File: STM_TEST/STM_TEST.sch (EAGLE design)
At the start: 49 parts, among them U1 TPS2115APWR, U2 AZ1117EH-3.3TRG1, Y1 ECS-80-S-4X, Y2 ECS-80-S-4X

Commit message: routing
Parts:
- removed C3, C4: 1.0uF, SparkFun-Capacitors:1.0UF-0603-16V-10%
- removed SW1: (no value), special:SW_DIP-2
- removed U2: AZ1117EH-3.3TRG1, AZ1117EH-3.3TRG1:AZ1117EH-3.3TRG1
- added R12: 10k, SparkFun-Resistors:100KOHM-0603-1/10W-1%
- added R13, R14: 10k, SparkFun-Resistors:1KOHM-0603-1/10W-1%
- R3, R4: device SparkFun-Resistors:100KOHM-0603-1/10W-1% -> SparkFun-Resistors:1KOHM-0603-1/10W-1%
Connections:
- removed net D1: R3.2, SW1.1, U1.D1
- removed net SCL: PCB1.GPIO3
- removed net SDA: PCB1.GPIO2
- removed net VCC: C3.1, J1.2, U2.IN
- new net +3V3ROV_ADC2: R3.1, R4.2, U$2.PA2
- new net +5V_ADC1: R13.1, R14.2, U$2.PA1
- net +3V3ROV: now also J1.2, R12.2, R3.2; no longer C4.1, R3.1, R4.1, U2.OUT
- net +5V: now also R13.2
- net D0: now also R12.1; no longer R4.2, SW1.2
- net GND: now also R14.1, R4.1, U1.D1; no longer C3.2, C4.2, SW1.3, SW1.4, U2.ADJ/GND
- net I2C1_SCL: now also PCB1.GPIO3
- net I2C1_SDA: now also PCB1.GPIO2

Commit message: uhhh, yeah boards looking good
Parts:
- added C3: 0.1uF, SparkFun-Capacitors:4.7UF0603
- added U$4: ACS711, ACS711_ameter:ACS711
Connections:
- new net +5V_TO_PI: U$4.IP1-, U$4.IP2-
- new net PI_CURRENT: U$2.PA0, U$4.VIOUT
- net +3V3: now also C3.1, U$4.VCC
- net +5V: now also U$4.IP1+, U$4.IP2+
- net GND: now also C3.2, U$4.GND
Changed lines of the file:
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@@
 <part name="R14" library="SparkFun-Resistors" library_urn="urn:adsk.eagle:library:532" deviceset="1KOHM" device="-0603-1/10W-1%" package3d_urn="urn:adsk.eagle:package:39650/1" value="10k"/>
 <part name="GND10" library="supply1" library_urn="urn:adsk.eagle:library:371" deviceset="GND" device=""/>
+<part name="U$4" library="ACS711_ameter" deviceset="ACS711" device=""/>
+<part name="C3" library="SparkFun-Capacitors" library_urn="urn:adsk.eagle:library:510" deviceset="4.7UF" device="0603" package3d_urn="urn:adsk.eagle:package:37414/1" value="0.1uF"/>
+<part name="GND17" library="supply1" library_urn="urn:adsk.eagle:library:371" deviceset="GND" device=""/>
+<part name="+3V7" library="supply1" library_urn="urn:adsk.eagle:library:371" deviceset="+3V3" device=""/>
 </parts>
 <sheets>
@@
 <instance part="GND10" gate="1" x="314.96" y="50.8">
 <attribute name="VALUE" x="312.42" y="48.26" size="1.778" layer="96"/>
+</instance>
+<instance part="U$4" gate="G$1" x="210.82" y="53.34"/>
+<instance part="C3" gate="G$1" x="251.46" y="53.34">
+<attribute name="NAME" x="252.984" y="56.261" size="1.778" layer="95" font="vector"/>
+<attribute name="VALUE" x="252.984" y="51.181" size="1.778" layer="96" font="vector"/>
+</instance>
+<instance part="GND17" gate="1" x="251.46" y="40.64">
+<attribute name="VALUE" x="248.92" y="38.1" size="1.778" layer="96"/>
+</instance>
+<instance part="+3V7" gate="G$1" x="251.46" y="78.74">
+<attribute name="VALUE" x="248.92" y="73.66" size="1.778" layer="96" rot="R90"/>
 </instance>
 </instances>
@@
 <wire x1="314.96" y1="60.96" x2="314.96" y2="53.34" width="0.1524" layer="91"/>
 </segment>
+<segment>
+<pinref part="C3" gate="G$1" pin="2"/>
+<pinref part="GND17" gate="1" pin="GND"/>
+<wire x1="251.46" y1="50.8" x2="251.46" y2="45.72" width="0.1524" layer="91"/>
+<pinref part="U$4" gate="G$1" pin="GND"/>
+<wire x1="251.46" y1="45.72" x2="251.46" y2="43.18" width="0.1524" layer="91"/>
+<wire x1="223.52" y1="45.72" x2="251.46" y2="45.72" width="0.1524" layer="91"/>
+<junction x="251.46" y="45.72"/>
+</segment>
 </net>
 <net name="+3V3" class="0">
@@
 <junction x="45.72" y="58.42"/>
 </segment>
+<segment>
+<pinref part="U$4" gate="G$1" pin="VCC"/>
+<pinref part="C3" gate="G$1" pin="1"/>
+<wire x1="223.52" y1="60.96" x2="251.46" y2="60.96" width="0.1524" layer="91"/>
+<wire x1="251.46" y1="60.96" x2="251.46" y2="58.42" width="0.1524" layer="91"/>
+<pinref part="+3V7" gate="G$1" pin="+3V3"/>
+<wire x1="251.46" y1="60.96" x2="251.46" y2="76.2" width="0.1524" layer="91"/>
+<junction x="251.46" y="60.96"/>
+</segment>
 </net>
 <net name="NRST" class="0">
@@
 <label x="314.96" y="96.52" size="1.778" layer="95"/>
 </segment>
+<segment>
+<pinref part="U$4" gate="G$1" pin="IP1+"/>
+<pinref part="U$4" gate="G$1" pin="IP2+"/>
+<wire x1="198.12" y1="60.96" x2="198.12" y2="55.88" width="0.1524" layer="91"/>
+<wire x1="198.12" y1="60.96" x2="177.8" y2="60.96" width="0.1524" layer="91"/>
+<junction x="198.12" y="60.96"/>
+<label x="177.8" y="60.96" size="1.778" layer="95"/>
+</segment>
 </net>
 <net name="+3V3ROV" class="0">
@@
 <wire x1="347.98" y1="96.52" x2="347.98" y2="86.36" width="0.1524" layer="91"/>
 <label x="347.98" y="96.52" size="1.778" layer="95"/>
+</segment>
+</net>
+<net name="PI_CURRENT" class="0">
+<segment>
+<pinref part="U$2" gate="G$1" pin="PA0"/>
+<wire x1="264.16" y1="203.2" x2="248.92" y2="203.2" width="0.1524" layer="91"/>
+<label x="243.84" y="203.2" size="1.778" layer="95"/>
+</segment>
+<segment>
+<pinref part="U$4" gate="G$1" pin="VIOUT"/>
+<wire x1="223.52" y1="55.88" x2="243.84" y2="55.88" width="0.1524" layer="91"/>
+<label x="231.14" y="55.88" size="1.778" layer="95"/>
+</segment>
+</net>
+<net name="+5V_TO_PI" class="0">
+<segment>
+<pinref part="U$4" gate="G$1" pin="IP1-"/>
+<pinref part="U$4" gate="G$1" pin="IP2-"/>
+<wire x1="198.12" y1="50.8" x2="198.12" y2="45.72" width="0.1524" layer="91"/>
+<wire x1="198.12" y1="45.72" x2="177.8" y2="45.72" width="0.1524" layer="91"/>
+<junction x="198.12" y="45.72"/>
+<label x="177.8" y="45.72" size="1.778" layer="95"/>
 </segment>
 </net>
@@
 <net name="+5V" class="0">
 <segment>
+<wire x1="40.64" y1="91.44" x2="40.64" y2="104.14" width="0.1524" layer="91"/>
+<pinref part="P+1" gate="1" pin="+5V"/>
+<pinref part="PCB1" gate="G$1" pin="5V@2"/>
+<wire x1="40.64" y1="91.44" x2="63.5" y2="91.44" width="0.1524" layer="91"/>
+</segment>
+<segment>
 <pinref part="PCB1" gate="G$1" pin="5V@4"/>
 <wire x1="63.5" y1="96.52" x2="58.42" y2="96.52" width="0.1524" layer="91"/>
-<wire x1="58.42" y1="96.52" x2="58.42" y2="93.98" width="0.1524" layer="91"/>
-<pinref part="PCB1" gate="G$1" pin="5V@2"/>
-<wire x1="58.42" y1="93.98" x2="58.42" y2="91.44" width="0.1524" layer="91"/>
-<wire x1="58.42" y1="91.44" x2="63.5" y2="91.44" width="0.1524" layer="91"/>
-<wire x1="58.42" y1="93.98" x2="40.64" y2="93.98" width="0.1524" layer="91"/>
-<wire x1="40.64" y1="93.98" x2="40.64" y2="104.14" width="0.1524" layer="91"/>
-<junction x="58.42" y="93.98"/>
-<pinref part="P+1" gate="1" pin="+5V"/>
-</segment>
-</net>
+<label x="55.88" y="96.52" size="1.778" layer="95"/>
+</segment>
+</net>

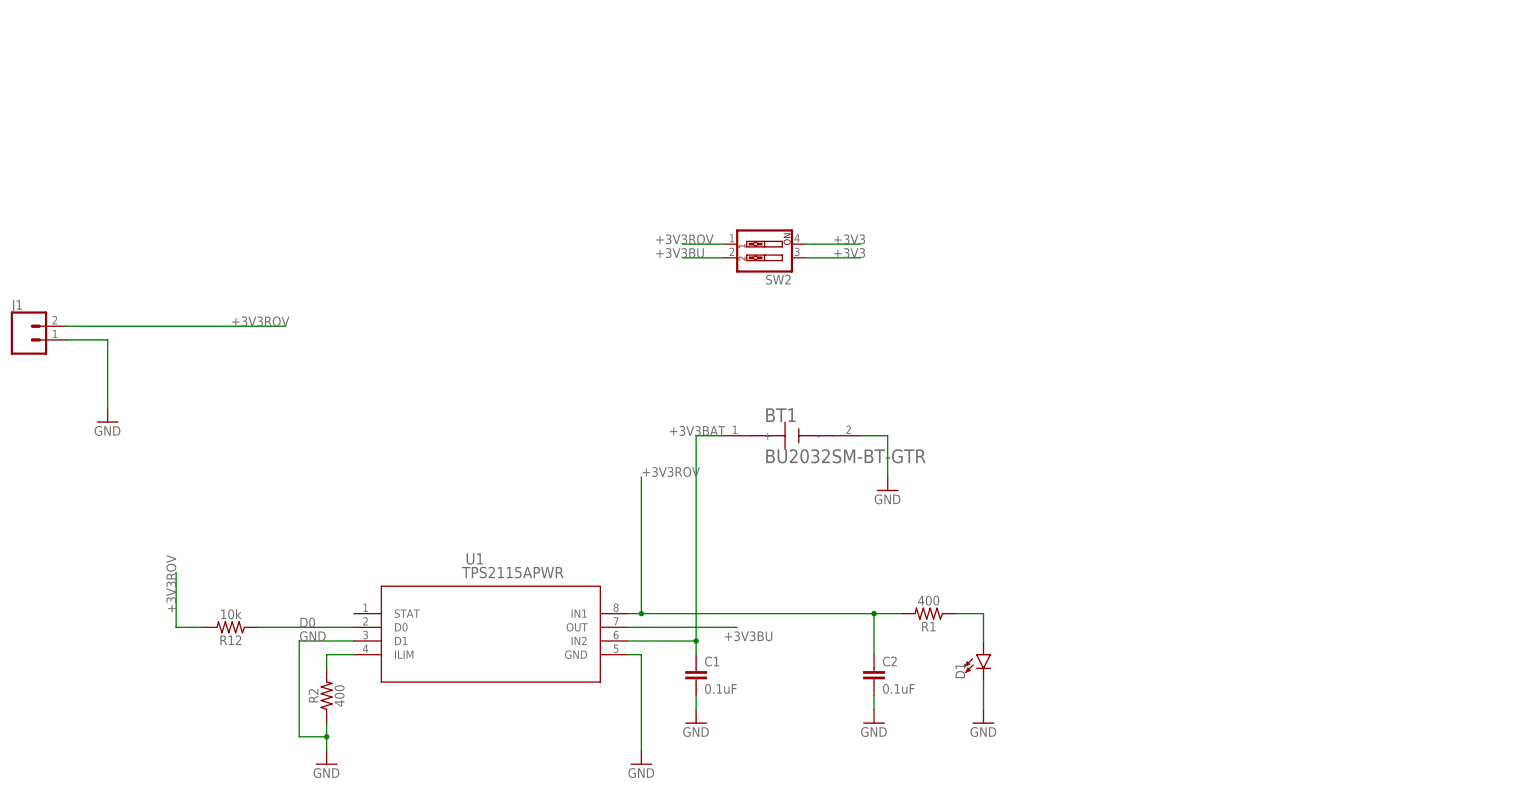
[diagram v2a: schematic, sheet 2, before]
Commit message: Routing Complete
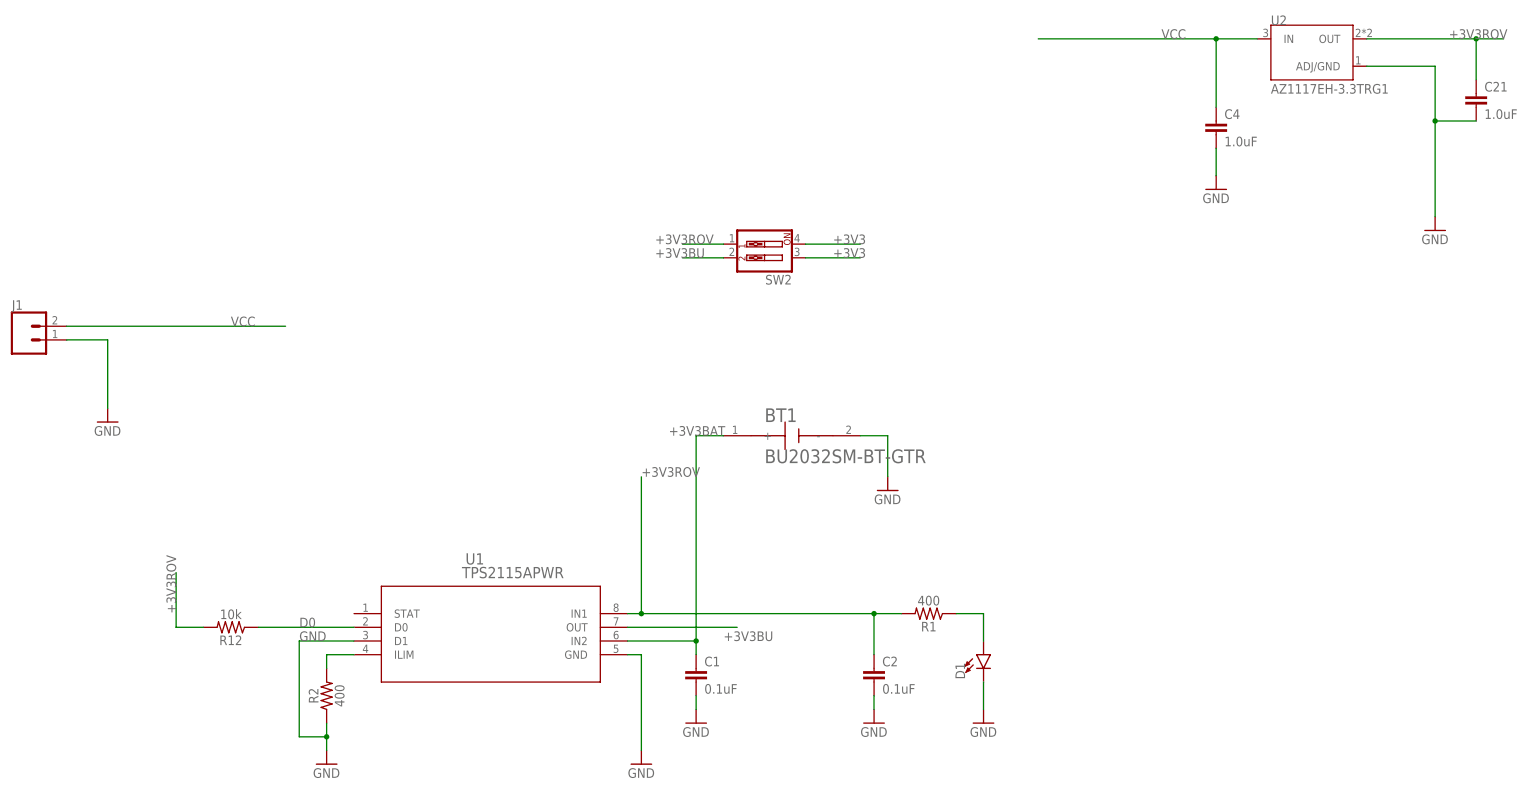
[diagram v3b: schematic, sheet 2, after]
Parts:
- added C21, C4: 1.0uF, SparkFun-Capacitors:1.0UF-0603-16V-10%
- added U2: AZ1117EH-3.3TRG1, AZ1117EH-3.3TRG1:AZ1117EH-3.3TRG1
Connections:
- removed net +5V_TO_PI: U$4.IP1-, U$4.IP2-
- new net VCC: C4.1, J1.2, U$4.IP1-, U$4.IP2-, U2.IN
- net +3V3ROV: now also C21.1, U2.OUT; no longer J1.2
- net GND: now also C21.2, C4.2, U2.ADJ/GND
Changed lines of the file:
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@@
 <part name="GND17" library="supply1" library_urn="urn:adsk.eagle:library:371" deviceset="GND" device=""/>
 <part name="+3V7" library="supply1" library_urn="urn:adsk.eagle:library:371" deviceset="+3V3" device=""/>
+<part name="U2" library="AZ1117EH-3.3TRG1" deviceset="AZ1117EH-3.3TRG1" device=""/>
+<part name="GND33" library="supply1" library_urn="urn:adsk.eagle:library:371" deviceset="GND" device=""/>
+<part name="C4" library="SparkFun-Capacitors" deviceset="1.0UF" device="-0603-16V-10%" value="1.0uF"/>
+<part name="C21" library="SparkFun-Capacitors" deviceset="1.0UF" device="-0603-16V-10%" value="1.0uF"/>
+<part name="GND34" library="supply1" library_urn="urn:adsk.eagle:library:371" deviceset="GND" device=""/>
 </parts>
 <sheets>
@@
 </segment>
 </net>
-<net name="+5V_TO_PI" class="0">
+<net name="VCC" class="0">
 <segment>
 <pinref part="U$4" gate="G$1" pin="IP1-"/>
@@
 <attribute name="VALUE" x="68.58" y="120.904" size="1.778" layer="96" font="vector" rot="R180" align="top-center"/>
 </instance>
+<instance part="U2" gate="G$1" x="269.24" y="226.06">
+<attribute name="NAME" x="261.61058125" y="231.14628125" size="1.7802" layer="95"/>
+<attribute name="VALUE" x="261.612559375" y="218.432559375" size="1.779740625" layer="96"/>
+</instance>
+<instance part="GND33" gate="1" x="292.1" y="193.04">
+<attribute name="VALUE" x="289.56" y="190.5" size="1.778" layer="96"/>
+</instance>
+<instance part="C4" gate="G$1" x="251.46" y="210.82">
+<attribute name="NAME" x="252.984" y="213.741" size="1.778" layer="95" font="vector"/>
+<attribute name="VALUE" x="252.984" y="208.661" size="1.778" layer="96" font="vector"/>
+</instance>
+<instance part="C21" gate="G$1" x="299.72" y="215.9">
+<attribute name="NAME" x="301.244" y="218.821" size="1.778" layer="95" font="vector"/>
+<attribute name="VALUE" x="301.244" y="213.741" size="1.778" layer="96" font="vector"/>
+</instance>
+<instance part="GND34" gate="1" x="251.46" y="200.66">
+<attribute name="VALUE" x="248.92" y="198.12" size="1.778" layer="96"/>
+</instance>
 </instances>
 <busses>
@@
 <wire x1="81.28" y1="99.06" x2="86.36" y2="99.06" width="0.1524" layer="91"/>
 <junction x="86.36" y="99.06"/>
+</segment>
+<segment>
+<pinref part="U2" gate="G$1" pin="ADJ/GND"/>
+<wire x1="279.4" y1="223.52" x2="292.1" y2="223.52" width="0.1524" layer="91"/>
+<wire x1="292.1" y1="223.52" x2="292.1" y2="213.36" width="0.1524" layer="91"/>
+<pinref part="GND33" gate="1" pin="GND"/>
+<pinref part="C21" gate="G$1" pin="2"/>
+<wire x1="292.1" y1="213.36" x2="292.1" y2="195.58" width="0.1524" layer="91"/>
+<wire x1="299.72" y1="213.36" x2="292.1" y2="213.36" width="0.1524" layer="91"/>
+<junction x="292.1" y="213.36"/>
+</segment>
+<segment>
+<pinref part="GND34" gate="1" pin="GND"/>
+<pinref part="C4" gate="G$1" pin="2"/>
+<wire x1="251.46" y1="203.2" x2="251.46" y2="208.28" width="0.1524" layer="91"/>
 </segment>
 </net>
@@
 </segment>
 <segment>
-<pinref part="J1" gate="G$1" pin="2"/>
-<wire x1="38.1" y1="175.26" x2="78.74" y2="175.26" width="0.1524" layer="91"/>
-<label x="68.58" y="175.26" size="1.778" layer="95"/>
+<pinref part="U2" gate="G$1" pin="OUT"/>
+<wire x1="279.4" y1="228.6" x2="299.72" y2="228.6" width="0.1524" layer="91"/>
+<pinref part="C21" gate="G$1" pin="1"/>
+<wire x1="299.72" y1="228.6" x2="304.8" y2="228.6" width="0.1524" layer="91"/>
+<wire x1="299.72" y1="220.98" x2="299.72" y2="228.6" width="0.1524" layer="91"/>
+<junction x="299.72" y="228.6"/>
+<label x="294.64" y="228.6" size="1.778" layer="95"/>
 </segment>
 </net>
@@
 </segment>
 </net>
+<net name="VCC" class="0">
+<segment>
+<pinref part="J1" gate="G$1" pin="2"/>
+<wire x1="38.1" y1="175.26" x2="78.74" y2="175.26" width="0.1524" layer="91"/>
+<label x="68.58" y="175.26" size="1.778" layer="95"/>
+</segment>
+<segment>
+<pinref part="U2" gate="G$1" pin="IN"/>
+<wire x1="259.08" y1="228.6" x2="251.46" y2="228.6" width="0.1524" layer="91"/>
+<pinref part="C4" gate="G$1" pin="1"/>
+<wire x1="251.46" y1="215.9" x2="251.46" y2="228.6" width="0.1524" layer="91"/>
+<junction x="251.46" y="228.6"/>
+<label x="241.3" y="228.6" size="1.778" layer="95"/>
+<wire x1="218.44" y1="228.6" x2="251.46" y2="228.6" width="0.1524" layer="91"/>
+</segment>
+</net>
